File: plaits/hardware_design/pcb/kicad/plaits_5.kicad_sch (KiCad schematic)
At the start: 26 parts

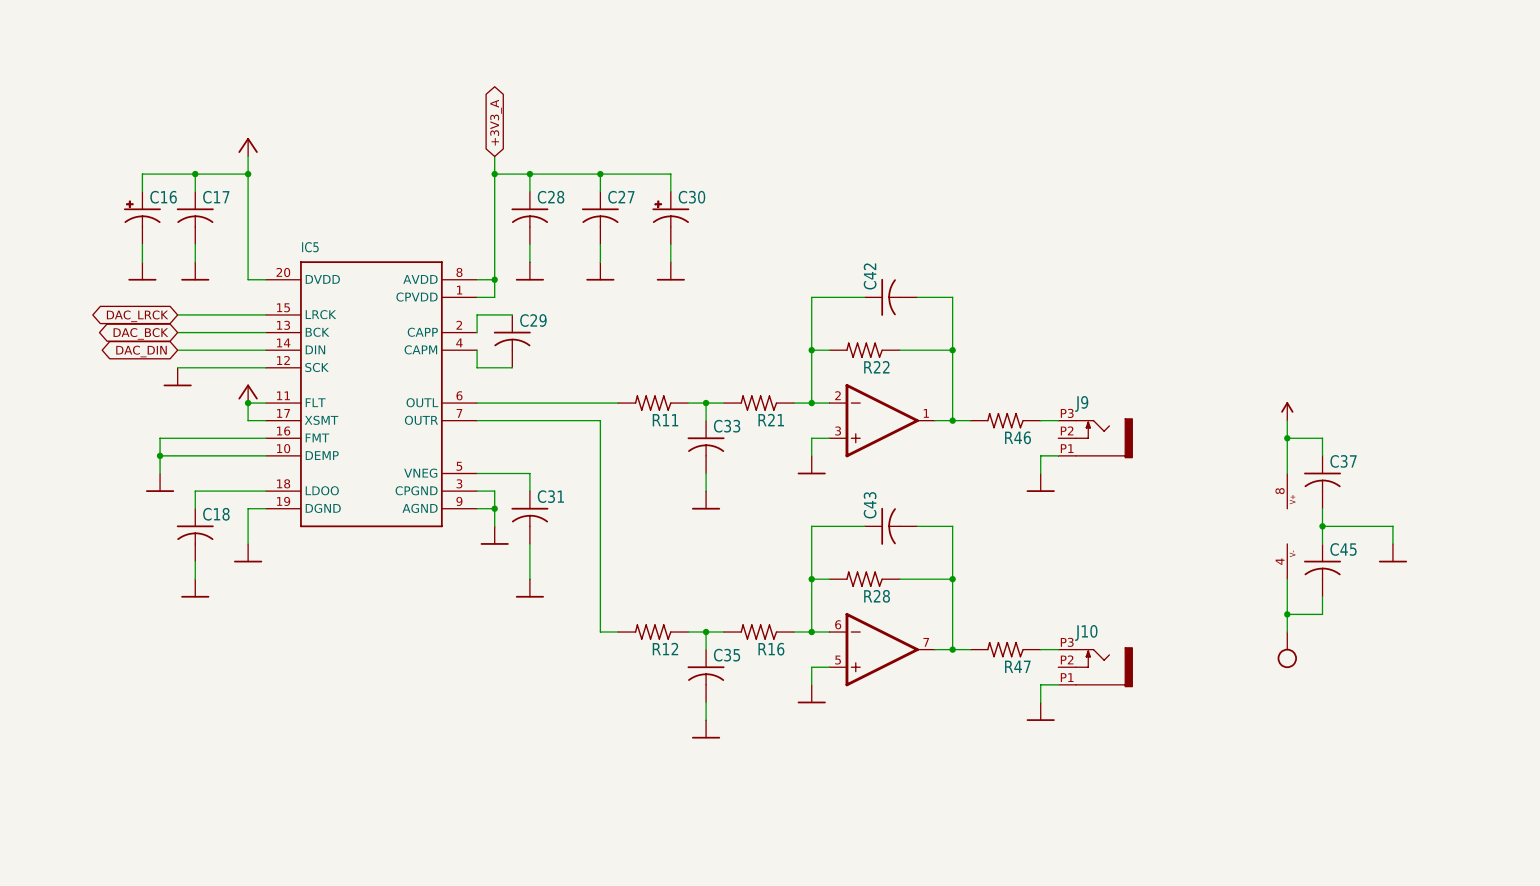
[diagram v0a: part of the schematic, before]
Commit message: plaits resized panasonic A -> B caps
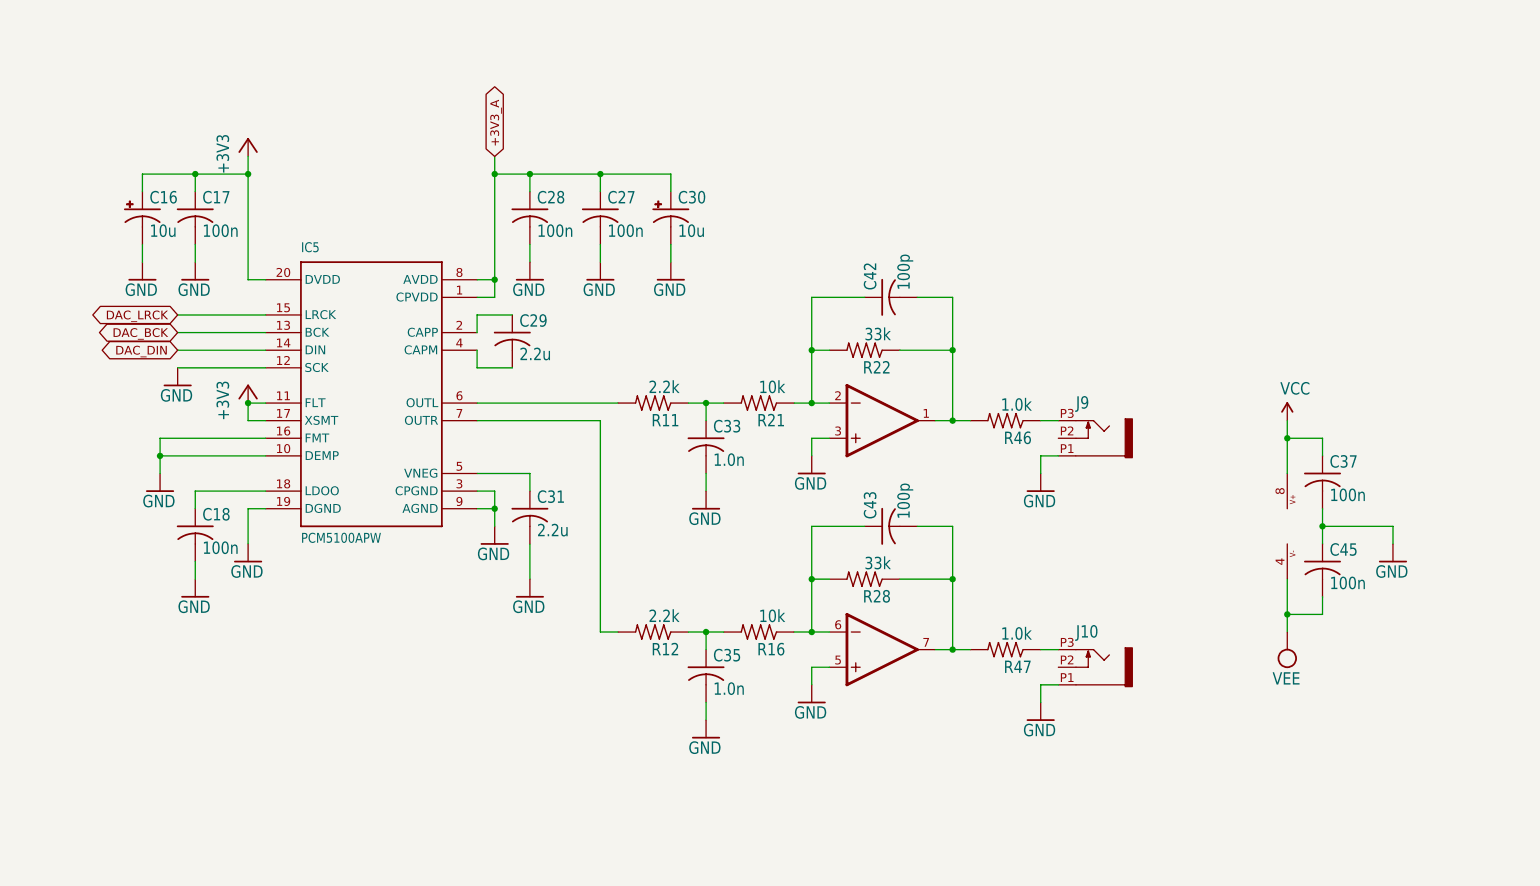
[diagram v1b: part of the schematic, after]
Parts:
- C16, C30: value (none) -> 10u; footprint (none) -> plaits:PANASONIC_B
- C17, C18, C27, C28, C37, C45: value (none) -> 100n; footprint (none) -> plaits:C0402
- C29, C31: value (none) -> 2.2u; footprint (none) -> plaits:C0805
- C33, C35: value (none) -> 1.0n; footprint (none) -> plaits:C0402
- C42, C43: value (none) -> 100p; footprint (none) -> plaits:C0402
- IC5: value (none) -> PCM5100APW; footprint (none) -> plaits:SSOP20
- IC8: value (none) -> TL072PW; footprint (none) -> plaits:TSSOP08
- J10, J9: value (none) -> PJ301_THONKICONN6; footprint (none) -> plaits:WQP_PJ_301M6
- R11, R12: value (none) -> 2.2k; footprint (none) -> plaits:R0402
- R16, R21: value (none) -> 10k; footprint (none) -> plaits:R0402
- R22, R28: value (none) -> 33k; footprint (none) -> plaits:R0402
- R46, R47: value (none) -> 1.0k; footprint (none) -> plaits:R0603
